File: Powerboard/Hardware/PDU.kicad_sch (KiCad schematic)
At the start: 42 parts, among them J1 Conn_01x03_MountingPin, J7 XT60PW-M, J8 Conn_01x04_Male, J9 XT60PW-M, U2 ESP32-S3, Y1 40MHz±10ppm

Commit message: added some commands, hardware fixes
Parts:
- 3V3LED1, TXLED1: footprint Resistor_SMD:R_0402_1005Metric -> LED_SMD:LED_0402_1005Metric
- BATTLED1: renamed from 12VLED1; value 12V_LED -> BATT_LED; footprint Resistor_SMD:R_0402_1005Metric -> LED_SMD:LED_0402_1005Metric
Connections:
- net DepVoltage: now reaches U2.18 (GPIO13/ADC2_CH2)
- net 12V_SWITCH renamed DEP_SWITCH
- net 3V3LOG renamed LogicVoltage
- net 3V3_SWITCH renamed LOGIC_SWITCH
- net DeploymentVoltage renamed BattVoltage
- net PDU_EN renamed ARMING
- no-connect marks 30 -> 29
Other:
- sheet Bucks ports: added LogicVoltage; removed 3V3LOG
- sheet Switches+RBUS ports: added DEP_SWITCH, DepVoltage, LOGIC_SWITCH; removed 12V_SWITCH, 3V3_SWITCH
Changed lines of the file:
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@@
   (no_connect (at 176.022 98.552))
   (no_connect (at 176.022 101.092))
-  (no_connect (at 176.022 103.632))
   (no_connect (at 242.062 111.252))
   (no_connect (at 242.062 101.092))
@@
     (effects (font (size 1.27 1.27)) (justify left bottom))
   )
-  (label "12V_SWITCH" (at 64.262 79.502 0) (fields_autoplaced)
-    (effects (font (size 1.27 1.27)) (justify left bottom))
-  )
   (label "LIPOPOWER" (at 242.062 118.872 0) (fields_autoplaced)
     (effects (font (size 1.27 1.27)) (justify left bottom))
@@
     (effects (font (size 1.27 1.27)) (justify right bottom))
   )
-  (label "3V3LOG" (at 78.74 50.546 180) (fields_autoplaced)
-    (effects (font (size 1.27 1.27)) (justify right bottom))
+  (label "LogicVoltage" (at 106.172 50.546 0) (fields_autoplaced)
+    (effects (font (size 1.27 1.27)) (justify left bottom))
   )
   (label "CAN-" (at 35.052 70.358 180) (fields_autoplaced)
     (effects (font (size 1.27 1.27)) (justify right bottom))
   )
-  (label "DeploymentVoltage" (at 65.786 148.844 0) (fields_autoplaced)
+  (label "BattVoltage" (at 65.786 148.844 0) (fields_autoplaced)
     (effects (font (size 1.27 1.27)) (justify left bottom))
   )
@@
     (effects (font (size 1.27 1.27)) (justify right bottom))
   )
-  (label "DeploymentVoltage" (at 176.022 106.172 180) (fields_autoplaced)
+  (label "BattVoltage" (at 176.022 106.172 180) (fields_autoplaced)
     (effects (font (size 1.27 1.27)) (justify right bottom))
   )
@@
     (effects (font (size 1.27 1.27)) (justify right bottom))
   )
-  (label "12V_SWITCH" (at 242.062 106.172 0) (fields_autoplaced)
+  (label "DEP_SWITCH" (at 242.062 106.172 0) (fields_autoplaced)
     (effects (font (size 1.27 1.27)) (justify left bottom))
   )
@@
     (effects (font (size 1.27 1.27)) (justify right bottom))
   )
-  (label "3V3_SWITCH" (at 242.062 103.632 0) (fields_autoplaced)
+  (label "LOGIC_SWITCH" (at 242.062 103.632 0) (fields_autoplaced)
     (effects (font (size 1.27 1.27)) (justify left bottom))
   )
@@
     (effects (font (size 1.27 1.27)) (justify right bottom))
   )
-  (label "USBPOWER" (at 106.172 39.878 0) (fields_autoplaced)
+  (label "DepVoltage" (at 64.262 67.31 0) (fields_autoplaced)
+    (effects (font (size 1.27 1.27)) (justify left bottom))
+  )
+  (label "DEP_SWITCH" (at 64.262 74.676 0) (fields_autoplaced)
+    (effects (font (size 1.27 1.27)) (justify left bottom))
+  )
+  (label "USBPOWER" (at 106.172 36.322 0) (fields_autoplaced)
     (effects (font (size 1.27 1.27)) (justify left bottom))
   )
@@
     (effects (font (size 1.27 1.27)) (justify left bottom))
   )
-  (label "PDU_EN" (at 242.062 96.012 0) (fields_autoplaced)
+  (label "ARMING" (at 242.062 96.012 0) (fields_autoplaced)
     (effects (font (size 1.27 1.27)) (justify left bottom))
   )
@@
     (effects (font (size 1.27 1.27)) (justify right bottom))
   )
-  (label "LIPOPOWER" (at 106.172 47.752 0) (fields_autoplaced)
-    (effects (font (size 1.27 1.27)) (justify left bottom))
-  )
-  (label "Data-" (at 87.122 112.522 0) (fields_autoplaced)
-    (effects (font (size 1.27 1.27)) (justify left bottom))
-  )
-  (label "3V3_SWITCH" (at 64.262 69.596 0) (fields_autoplaced)
+  (label "LIPOPOWER" (at 106.172 43.942 0) (fields_autoplaced)
+    (effects (font (size 1.27 1.27)) (justify left bottom))
+  )
+  (label "Data-" (at 85.09 105.41 0) (fields_autoplaced)
+    (effects (font (size 1.27 1.27)) (justify left bottom))
+  )
+  (label "LOGIC_SWITCH" (at 64.262 82.55 0) (fields_autoplaced)
     (effects (font (size 1.27 1.27)) (justify left bottom))
   )
@@
     (effects (font (size 1.27 1.27)) (justify right bottom))
   )
-  (label "PDU_EN" (at 29.718 146.812 0) (fields_autoplaced)
+  (label "ARMING" (at 29.718 146.812 0) (fields_autoplaced)
     (effects (font (size 1.27 1.27)) (justify left bottom))
   )
@@
     (effects (font (size 1.27 1.27)) (justify left bottom))
   )
-  (label "3V3LOG" (at 176.022 85.852 180) (fields_autoplaced)
+  (label "LogicVoltage" (at 176.022 85.852 180) (fields_autoplaced)
     (effects (font (size 1.27 1.27)) (justify right bottom))
   )
@@
     (effects (font (size 1.27 1.27)) (justify right bottom))
   )
-  (label "Data+" (at 87.122 106.68 0) (fields_autoplaced)
-    (effects (font (size 1.27 1.27)) (justify left bottom))
+  (label "Data+" (at 85.09 114.3 0) (fields_autoplaced)
+    (effects (font (size 1.27 1.27)) (justify left bottom))
+  )
+  (label "DepVoltage" (at 176.022 103.632 180) (fields_autoplaced)
+    (effects (font (size 1.27 1.27)) (justify right bottom))
   )
   (symbol (lib_id "Mechanical:MountingHole_Pad") (at 39.878 181.356 0) (unit 1)
@@
   (symbol (lib_id "Device:LED_Small") (at 169.672 27.432 0) (unit 1)
     (in_bom yes) (on_board yes) (dnp no)
-    (property "Reference" "12VLED1" (at 169.672 32.639 0)
-      (effects (font (size 1.27 1.27)))
-    )
-    (property "Value" "12V_LED" (at 169.672 30.3276 0)
-      (effects (font (size 1.27 1.27)))
-    )
-    (property "Footprint" "Resistor_SMD:R_0402_1005Metric" (at 169.672 27.432 90)
+    (property "Reference" "BATTLED1" (at 169.672 32.639 0)
+      (effects (font (size 1.27 1.27)))
+    )
+    (property "Value" "BATT_LED" (at 169.672 30.3276 0)
+      (effects (font (size 1.27 1.27)))
+    )
+    (property "Footprint" "LED_SMD:LED_0402_1005Metric" (at 169.672 27.432 90)
       (effects (font (size 1.27 1.27)) hide)
     )
@@
       (project "Switcher"
         (path "/e63e39d7-6ac0-4ffd-8aa3-1841a4541b55"
-          (reference "12VLED1") (unit 1)
+          (reference "BATTLED1") (unit 1)
         )
       )
@@
       (effects (font (size 1.27 1.27)))
     )
-    (property "Footprint" "Resistor_SMD:R_0402_1005Metric" (at 160.782 22.352 90)
+    (property "Footprint" "LED_SMD:LED_0402_1005Metric" (at 160.782 22.352 90)
       (effects (font (size 1.27 1.27)) hide)
     )
@@
       (effects (font (size 1.27 1.27)))
     )
-    (property "Footprint" "Resistor_SMD:R_0402_1005Metric" (at 131.572 31.242 90)
+    (property "Footprint" "LED_SMD:LED_0402_1005Metric" (at 131.572 31.242 90)
       (effects (font (size 1.27 1.27)) hide)
     )
@@
       (effects (font (size 1.27 1.27)) (justify left top))
     )
-    (pin "3V3_SWITCH" input (at 64.262 69.596 0)
+    (pin "CAN-" bidirectional (at 35.052 70.358 180)
+      (effects (font (size 1.27 1.27)) (justify left))
+    )
+    (pin "CAN+" bidirectional (at 35.052 78.74 180)
+      (effects (font (size 1.27 1.27)) (justify left))
+    )
+    (pin "DEP_SWITCH" input (at 64.262 74.676 0)
       (effects (font (size 1.27 1.27)) (justify right))
     )
-    (pin "12V_SWITCH" input (at 64.262 79.502 0)
+    (pin "DepVoltage" output (at 64.262 67.31 0)
       (effects (font (size 1.27 1.27)) (justify right))
     )
-    (pin "CAN-" input (at 35.052 70.358 180)
-      (effects (font (size 1.27 1.27)) (justify left))
-    )
-    (pin "CAN+" input (at 35.052 78.74 180)
-      (effects (font (size 1.27 1.27)) (justify left))
+    (pin "LOGIC_SWITCH" input (at 64.262 82.55 0)
+      (effects (font (size 1.27 1.27)) (justify right))
     )
     (instances
@@
     )
   )
-  (sheet (at 57.404 100.33) (size 29.718 20.066) (fields_autoplaced)
+  (sheet (at 56.134 100.33) (size 28.956 20.066) (fields_autoplaced)
     (stroke (width 0.1524) (type solid))
     (fill (color 0 0 0 0.0000))
-    (property "Sheetname" "USB" (at 57.404 99.6184 0)
+    (property "Sheetname" "USB" (at 56.134 99.6184 0)
       (effects (font (size 1.27 1.27)) (justify left bottom))
     )
-    (property "Sheetfile" "usb.kicad_sch" (at 57.404 120.9806 0)
+    (property "Sheetfile" "usb.kicad_sch" (at 56.134 120.9806 0)
       (effects (font (size 1.27 1.27)) (justify left top))
     )
-    (pin "Data-" bidirectional (at 87.122 106.68 0)
+    (pin "Data-" bidirectional (at 85.09 105.41 0)
       (effects (font (size 1.27 1.27)) (justify right))
     )
-    (pin "Data+" bidirectional (at 87.122 112.522 0)
+    (pin "Data+" bidirectional (at 85.09 114.3 0)
       (effects (font (size 1.27 1.27)) (justify right))
     )
@@
       (effects (font (size 1.27 1.27)) (justify left top))
     )
-    (pin "USBPOWER" input (at 106.172 39.878 0)
+    (pin "USBPOWER" input (at 106.172 36.322 0)
       (effects (font (size 1.27 1.27)) (justify right))
     )
-    (pin "LIPOPOWER" input (at 106.172 47.752 0)
+    (pin "LIPOPOWER" input (at 106.172 43.942 0)
       (effects (font (size 1.27 1.27)) (justify right))
     )
-    (pin "3V3LOG" input (at 78.74 50.546 180)
-      (effects (font (size 1.27 1.27)) (justify left))
-    )
-    (instances
+    (pin "LogicVoltage" input (at 106.172 50.546 0)
+      (effects (font (size 1.27 1.27)) (justify right))
+    )
+    (instances

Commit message: firmware updates
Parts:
- added J2: FAN, Connector_PinHeader_2.54mm:PinHeader_1x02_P2.54mm_Vertical, symbol Connector:Conn_01x02_Pin
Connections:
- net +3V3: now also J2.1 (Pin_1)
- net GND: now also J2.2 (Pin_2)

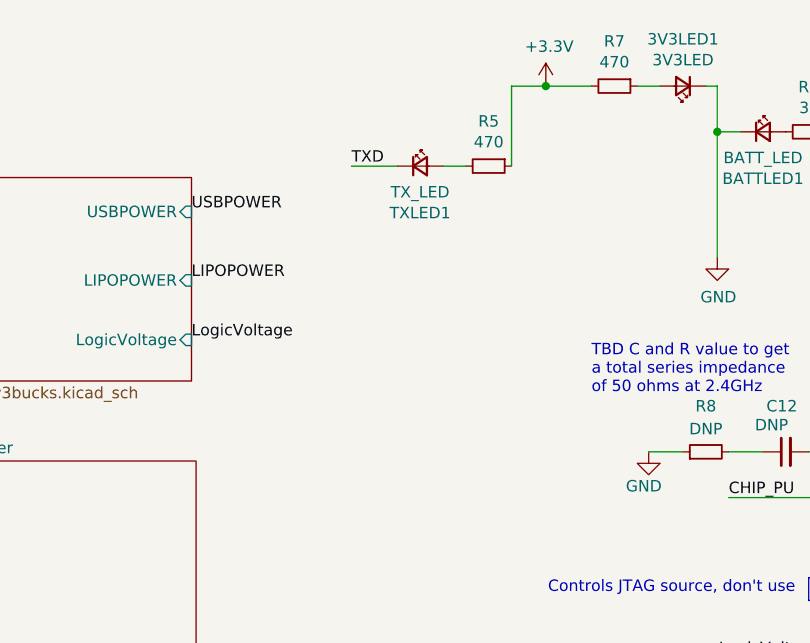
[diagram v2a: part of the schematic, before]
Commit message: can hardware fix, firmware updates
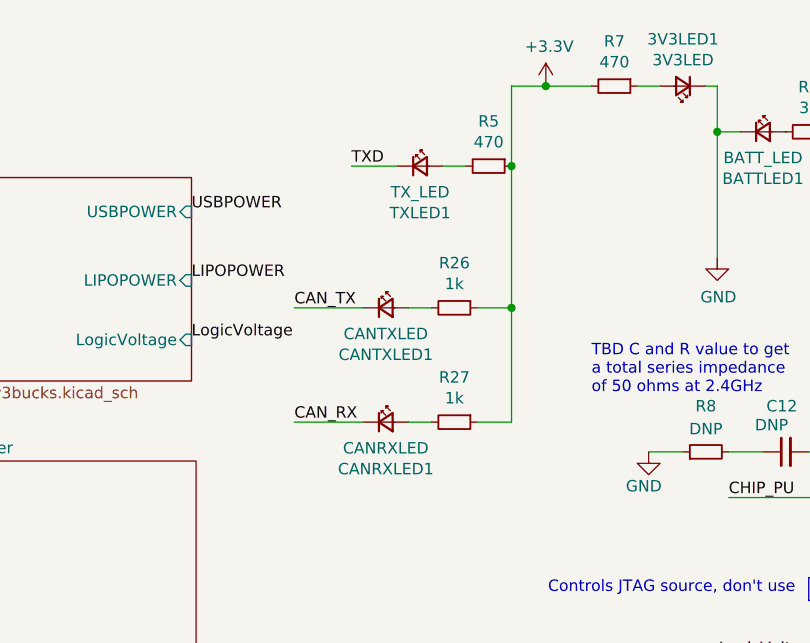
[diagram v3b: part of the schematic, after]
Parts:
- added CANRXLED1: CANRXLED, LED_SMD:LED_0402_1005Metric, symbol Device:LED_Small
- added CANTXLED1: CANTXLED, LED_SMD:LED_0402_1005Metric, symbol Device:LED_Small
- added R26, R27: 1k, Resistor_SMD:R_0402_1005Metric, symbol Device:R_Small
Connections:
- net +3V3: now also R26.1, R27.1
- net CAN_RX: now also CANRXLED1.1 (K)
- net CAN_TX: now also CANTXLED1.1 (K)
- new net: CANRXLED1.2 (A), R27.2
- new net: CANTXLED1.2 (A), R26.2
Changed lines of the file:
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@@
   (junction (at 135.382 136.652) (diameter 0) (color 0 0 0 0)
   )
+  (junction (at 141.732 46.99) (diameter 0) (color 0 0 0 0)
+  )
   (junction (at 159.512 132.842) (diameter 0) (color 0 0 0 0)
   )
@@
   )
   (junction (at 145.542 22.352) (diameter 0) (color 0 0 0 0)
+  )
+  (junction (at 141.732 31.242) (diameter 0) (color 0 0 0 0)
   )
   (junction (at 136.652 192.532) (diameter 0) (color 0 0 0 0)
@@
     (stroke (width 0) (type default))
   )
+  (wire (pts (xy 130.302 59.69) (xy 132.842 59.69))
+    (stroke (width 0) (type default))
+  )
   (wire (pts (xy 262.382 136.652) (xy 262.382 139.192))
     (stroke (width 0) (type default))
@@
     (stroke (width 0) (type default))
   )
+  (wire (pts (xy 141.732 59.69) (xy 137.922 59.69))
+    (stroke (width 0) (type default))
+  )
   (wire (pts (xy 122.682 192.532) (xy 126.492 192.532))
     (stroke (width 0) (type default))
@@
     (stroke (width 0) (type default))
   )
+  (wire (pts (xy 130.302 46.99) (xy 132.842 46.99))
+    (stroke (width 0) (type default))
+  )
   (wire (pts (xy 165.862 62.992) (xy 169.672 62.992))
     (stroke (width 0) (type default))
@@
     (stroke (width 0) (type default))
   )
+  (wire (pts (xy 141.732 31.242) (xy 141.732 46.99))
+    (stroke (width 0) (type default))
+  )
   (wire (pts (xy 43.688 183.896) (xy 46.228 183.896))
     (stroke (width 0) (type default))
@@
     (stroke (width 0) (type default))
   )
+  (wire (pts (xy 117.602 46.99) (xy 125.222 46.99))
+    (stroke (width 0) (type default))
+  )
   (wire (pts (xy 176.022 143.002) (xy 176.022 141.732))
     (stroke (width 0) (type default))
@@
     (stroke (width 0) (type default))
   )
+  (wire (pts (xy 141.732 46.99) (xy 137.922 46.99))
+    (stroke (width 0) (type default))
+  )
   (wire (pts (xy 164.592 22.352) (xy 164.592 27.432))
     (stroke (width 0) (type default))
@@
     (stroke (width 0) (type default))
   )
+  (wire (pts (xy 141.732 46.99) (xy 141.732 59.69))
+    (stroke (width 0) (type default))
+  )
   (wire (pts (xy 164.592 116.332) (xy 176.022 116.332))
     (stroke (width 0) (type default))
@@
   )
   (wire (pts (xy 145.542 22.352) (xy 150.622 22.352))
+    (stroke (width 0) (type default))
+  )
+  (wire (pts (xy 117.602 59.69) (xy 125.222 59.69))
     (stroke (width 0) (type default))
   )
@@
     (effects (font (size 1.27 1.27)) (justify right bottom))
   )
+  (label "CAN_RX" (at 117.602 59.69 0) (fields_autoplaced)
+    (effects (font (size 1.27 1.27)) (justify left bottom))
+  )
   (label "LOGIC_SWITCH" (at 242.062 103.632 0) (fields_autoplaced)
     (effects (font (size 1.27 1.27)) (justify left bottom))
@@
   )
   (label "DEP_SWITCH" (at 64.262 74.676 0) (fields_autoplaced)
+    (effects (font (size 1.27 1.27)) (justify left bottom))
+  )
+  (label "CAN_TX" (at 117.602 46.99 0) (fields_autoplaced)
     (effects (font (size 1.27 1.27)) (justify left bottom))
   )
@@
     )
   )
+  (symbol (lib_id "Device:R_Small") (at 135.382 59.69 270) (unit 1)
+    (in_bom yes) (on_board yes) (dnp no)
+    (property "Reference" "R27" (at 135.382 54.7116 90)
+      (effects (font (size 1.27 1.27)))
+    )
+    (property "Value" "1k" (at 135.382 57.023 90)
+      (effects (font (size 1.27 1.27)))
+    )
+    (property "Footprint" "Resistor_SMD:R_0402_1005Metric" (at 135.382 59.69 0)
+      (effects (font (size 1.27 1.27)) hide)
+    )
+    (property "Datasheet" "~" (at 135.382 59.69 0)
+      (effects (font (size 1.27 1.27)) hide)
+    )
+    (pin "1")
+    (pin "2")
+    (instances
+      (project "Chad"
+        (path "/7db990e4-92e1-4f99-b4d2-435bbec1ba83"
+          (reference "R27") (unit 1)
+        )
+      )
+      (project "PDU"
+        (path "/e63e39d7-6ac0-4ffd-8aa3-1841a4541b55"
+          (reference "R36") (unit 1)
+        )
+      )
+    )
+  )
   (symbol (lib_id "Device:C_Small") (at 163.322 145.542 0) (unit 1)
     (in_bom yes) (on_board yes) (dnp no)
@@
         (path "/e63e39d7-6ac0-4ffd-8aa3-1841a4541b55"
           (reference "#PWR0114") (unit 1)
+        )
+      )
+    )
+  )
+  (symbol (lib_id "Device:LED_Small") (at 127.762 59.69 0) (unit 1)
+    (in_bom yes) (on_board yes) (dnp no)
+    (property "Reference" "CANRXLED1" (at 127.762 64.897 0)
+      (effects (font (size 1.27 1.27)))
+    )
+    (property "Value" "CANRXLED" (at 127.762 62.5856 0)
+      (effects (font (size 1.27 1.27)))
+    )
+    (property "Footprint" "LED_SMD:LED_0402_1005Metric" (at 127.762 59.69 90)
+      (effects (font (size 1.27 1.27)) hide)
+    )
+    (property "Datasheet" "~" (at 127.762 59.69 90)
+      (effects (font (size 1.27 1.27)) hide)
+    )
+    (pin "1")
+    (pin "2")
+    (instances
+      (project "Chad"
+        (path "/7db990e4-92e1-4f99-b4d2-435bbec1ba83"
+          (reference "CANRXLED1") (unit 1)
+        )
+      )
+      (project "PDU"
+        (path "/e63e39d7-6ac0-4ffd-8aa3-1841a4541b55"
+          (reference "CANRXLED1") (unit 1)
         )
       )
@@
     )
   )
+  (symbol (lib_id "Device:LED_Small") (at 127.762 46.99 0) (unit 1)
+    (in_bom yes) (on_board yes) (dnp no)
+    (property "Reference" "CANTXLED1" (at 127.762 52.197 0)
+      (effects (font (size 1.27 1.27)))
+    )
+    (property "Value" "CANTXLED" (at 127.762 49.8856 0)
+      (effects (font (size 1.27 1.27)))
+    )
+    (property "Footprint" "LED_SMD:LED_0402_1005Metric" (at 127.762 46.99 90)
+      (effects (font (size 1.27 1.27)) hide)
+    )
+    (property "Datasheet" "~" (at 127.762 46.99 90)
+      (effects (font (size 1.27 1.27)) hide)
+    )
+    (pin "1")
+    (pin "2")
+    (instances
+      (project "Chad"
+        (path "/7db990e4-92e1-4f99-b4d2-435bbec1ba83"
+          (reference "CANTXLED1") (unit 1)
+        )
+      )
+      (project "PDU"
+        (path "/e63e39d7-6ac0-4ffd-8aa3-1841a4541b55"
+          (reference "CANTXLED1") (unit 1)
+        )
+      )
+    )
+  )
   (symbol (lib_id "power:GND") (at 151.892 172.212 0) (unit 1)
     (in_bom yes) (on_board yes) (dnp no)
@@
         )
       )
+    )
+  )
+  (symbol (lib_id "Device:R_Small") (at 135.382 46.99 270) (unit 1)
+    (in_bom yes) (on_board yes) (dnp no)
+    (property "Reference" "R26" (at 135.382 42.0116 90)
+      (effects (font (size 1.27 1.27)))
+    )
+    (property "Value" "1k" (at 135.382 44.323 90)
+      (effects (font (size 1.27 1.27)))
+    )
+    (property "Footprint" "Resistor_SMD:R_0402_1005Metric" (at 135.382 46.99 0)
+      (effects (font (size 1.27 1.27)) hide)
+    )
+    (property "Datasheet" "~" (at 135.382 46.99 0)
+      (effects (font (size 1.27 1.27)) hide)
+    )
+    (pin "1")
+    (pin "2")
+    (instances
+      (project "Chad"
+        (path "/7db990e4-92e1-4f99-b4d2-435bbec1ba83"
+          (reference "R26") (unit 1)
+        )
+      )
+      (project "PDU"
+        (path "/e63e39d7-6ac0-4ffd-8aa3-1841a4541b55"
+          (reference "R19") (unit 1)
+        )
+      )

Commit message: v2.1 ordering
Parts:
- 3V3LED1: value 3V3LED -> CYAN_LED
- BATTLED1: value BATT_LED -> ORANGE_LED
- C13, C14: value C -> 11pF
- CANRXLED1: value CANRXLED -> ORANGE_LED
- CANTXLED1: value CANTXLED -> EMERALD_LED
- TXLED1: value TX_LED -> GREEN_LED
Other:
- note removed: "TBD C and R value to get a total series impedance of 50 ohms at 2.4GHz"
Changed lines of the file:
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@@
     (effects (font (size 1.27 1.27)) (justify right bottom))
-  )
-  (text "TBD C and R value to get\na total series impedance\nof 50 ohms at 2.4GHz\n"
-    (at 150.622 56.642 0)
-    (effects (font (size 1.27 1.27)) (justify left bottom))
   )
   (text "Controls bootmode, don't use.\n" (at 244.7614 114.7377 0)
@@
       (effects (font (size 1.27 1.27)) (justify left))
     )
-    (property "Value" "C" (at 270.002 124.9934 90)
+    (property "Value" "11pF" (at 270.002 124.9934 90)
       (effects (font (size 1.27 1.27)) (justify left))
     )
@@
       (effects (font (size 1.27 1.27)))
     )
-    (property "Value" "BATT_LED" (at 169.672 30.3276 0)
+    (property "Value" "ORANGE_LED" (at 169.672 30.3276 0)
       (effects (font (size 1.27 1.27)))
     )
@@
       (effects (font (size 1.27 1.27)))
     )
-    (property "Value" "CANRXLED" (at 127.762 62.5856 0)
+    (property "Value" "ORANGE_LED" (at 127.762 62.5856 0)
       (effects (font (size 1.27 1.27)))
     )
@@
       (effects (font (size 1.27 1.27)))
     )
-    (property "Value" "CANTXLED" (at 127.762 49.8856 0)
+    (property "Value" "EMERALD_LED" (at 127.762 49.8856 0)
       (effects (font (size 1.27 1.27)))
     )
@@
       (effects (font (size 1.27 1.27)))
     )
-    (property "Value" "3V3LED" (at 160.782 19.4564 0)
+    (property "Value" "CYAN_LED" (at 160.782 19.4564 0)
       (effects (font (size 1.27 1.27)))
     )
@@
       (effects (font (size 1.27 1.27)))
     )
-    (property "Value" "TX_LED" (at 131.572 34.1376 0)
+    (property "Value" "GREEN_LED" (at 131.572 34.1376 0)
       (effects (font (size 1.27 1.27)))
     )
@@
       (effects (font (size 1.27 1.27)) (justify left))
     )
-    (property "Value" "C" (at 271.272 145.3134 90)
-      (effects (font (size 1.27 1.27)) (justify left))
-    )
+    (property "Value" "11pF" (at 271.272 145.3134 90)
+      (effects (font (size 1.27 1.27)) (justify left))
+    )

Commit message: v2.2 hardware
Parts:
- removed J2: FAN, Connector_PinHeader_2.54mm:PinHeader_1x02_P2.54mm_Vertical, symbol Connector:Conn_01x02_Pin
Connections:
- net DEP_SWITCH renamed DepSwitch
- net LIPOPOWER: no longer names the net of U2.37 (SPICLK_P/GPIO47)
- net LOGIC_SWITCH renamed LogicSwitch
- net USBPOWER: no longer names the net of U2.36 (SPICLK_N/GPIO48)
- no-connect marks 29 -> 31
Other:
- sheet Bucks ports: added none; removed LIPOPOWER, LogicVoltage, USBPOWER
- sheet Switches+RBUS ports: added DepSwitch, LogicSwitch, LogicVoltage; removed DEP_SWITCH, LOGIC_SWITCH

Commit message: commit before trying to squish the layout
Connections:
- net ARMING: now also J1.2 (Pin_2), J1.3 (Pin_3), J1.MP (MountPin); no longer J1.1 (Pin_1)
- net GND: now also J1.1 (Pin_1); no longer J1.2 (Pin_2), J1.3 (Pin_3), J1.MP (MountPin)
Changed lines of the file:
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@@
 	)
 	(label "ARMING"
-		(at 29.718 146.812 0)
+		(at 39.878 141.478 270)
 		(fields_autoplaced yes)
 		(effects
@@
 				(size 1.27 1.27)
 			)
-			(justify left bottom)
+			(justify right bottom)
 		)
 	)
@@
 	(symbol
 		(lib_id "power:GND")
-		(at 39.878 141.478 0)
+		(at 29.718 146.812 0)
 		(unit 1)
 		(exclude_from_sim no)
@@
 		(dnp no)
 		(property "Reference" "#PWR0101"
-			(at 39.878 147.828 0)
+			(at 29.718 153.162 0)
 			(effects
 				(font
@@
 		)
 		(property "Value" "GND"
-			(at 40.005 145.8722 0)
+			(at 29.845 151.2062 0)
 			(effects
 				(font
@@
 		)
 		(property "Footprint" ""
-			(at 39.878 141.478 0)
+			(at 29.718 146.812 0)
 			(effects
 				(font
@@
 		)
 		(property "Datasheet" ""
-			(at 39.878 141.478 0)
+			(at 29.718 146.812 0)
 			(effects
 				(font
@@
 		)
 		(property "Description" ""
-			(at 39.878 141.478 0)
+			(at 29.718 146.812 0)
 			(effects
 				(font
